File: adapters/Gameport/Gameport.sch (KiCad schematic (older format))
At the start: 20 parts, among them J1 Port 1, J2 Port 2, J3 Gameport, M1 Mounting, M2 Mounting, M3 Mounting, M4 Mounting, Q1 BC557, Q2 BC557

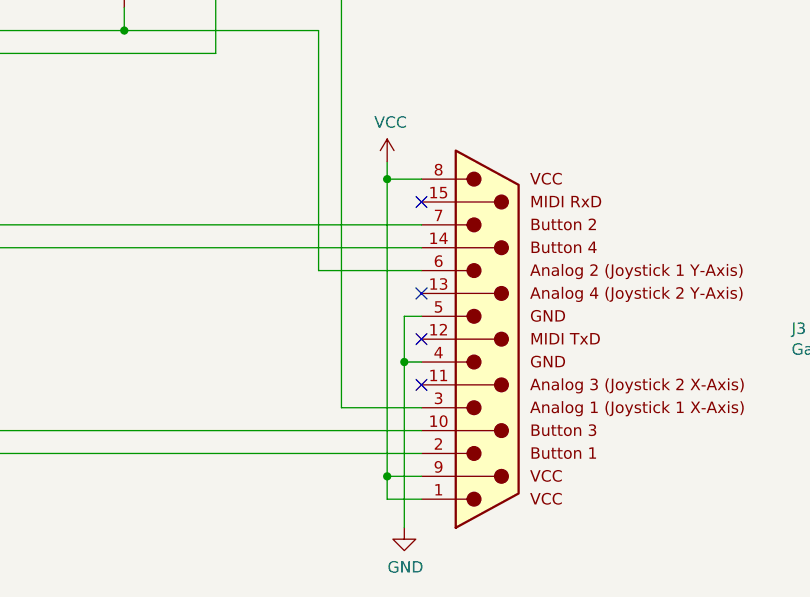
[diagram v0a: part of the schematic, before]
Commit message: Fixed pin linked to VCC
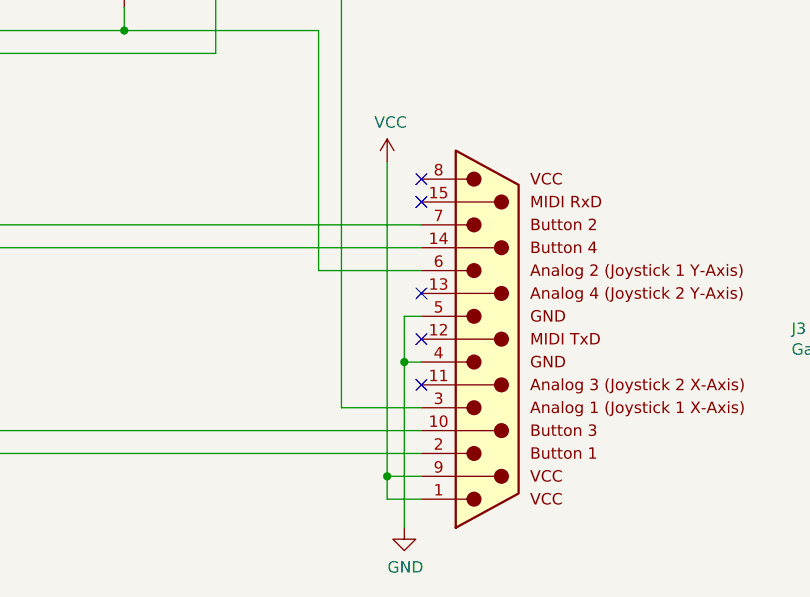
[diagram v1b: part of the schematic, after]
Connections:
- net VCC: no longer J3.8 (VCC)
- no-connect marks 13 -> 14
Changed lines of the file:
@@
 Rev "A"
 Comp ""
-Comment1 "Adapter is untested!"
+Comment1 ""
 Comment2 "Gravis gamepad makes this a viable option for many games."
 Comment3 "gameport. While originally an analog controller, the adoption of gamepads such as the"
@@
 	1    0    0    -1
 $EndComp
-Wire Wire Line
-	8450 4450 8450 4375
 $Comp
 L pc_gameport:Gameport_DB15 J3
@@
 $EndComp
 Wire Wire Line
-	8450 4450 8450 5750
-Connection ~ 8450 4450
-Wire Wire Line
 	8450 5750 8450 5850
 Connection ~ 8450 5750
-Wire Wire Line
-	8450 4450 8600 4450
 Wire Wire Line
 	8450 5750 8600 5750
@@
 Wire Wire Line
 	3025 1550 3025 1950
+Wire Wire Line
+	8450 4375 8450 5750
+NoConn ~ 8600 4450
 $EndSCHEMATC

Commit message: Trying out different circuit
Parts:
- removed Q1, Q2: BC557, Package_TO_SOT_THT:TO-92_Inline_Wide, symbol Transistor_BJT:BC557
- removed RV1, RV2: 100k, RM-065:RM-065, symbol Device:R_POT
- added Q1, Q2: 2N3906, Package_TO_SOT_THT:TO-92_Inline_Wide, symbol Transistor_BJT:2N3906
- added R7, R8: 100k, resistor:R_Axial_DIN0207_L6.3mm_D2.5mm_P7.62mm_Horizontal, symbol Device:R
- R1, R2: value 2k2 -> 100k
- R5, R6: value 2k2 -> 47k
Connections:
- net JK_DOWN: now also R2.2; no longer R6.2
- net JK_LEFT: now also R5.1; no longer R1.2, R3.2
- net JK_RIGHT: now also R1.2; no longer R5.2
- net JK_UP: now also R6.2; no longer R2.2, R4.2
- net VCC: now also R3.1, R4.1, Q1.1 (E), Q2.1 (E), R7.1, R8.1; no longer J3.9 (VCC), R5.1, R6.1
- net at J3.3 (A1): now also D1.1 (K), R3.2, Q1.3 (C)
- net at J3.6 (A2): now also D2.1 (K), R4.2, Q2.3 (C)
- new net: Q1.2 (B), R5.2, R7.2
- new net: Q2.2 (B), R6.1, R8.2
- no-connect marks 14 -> 15

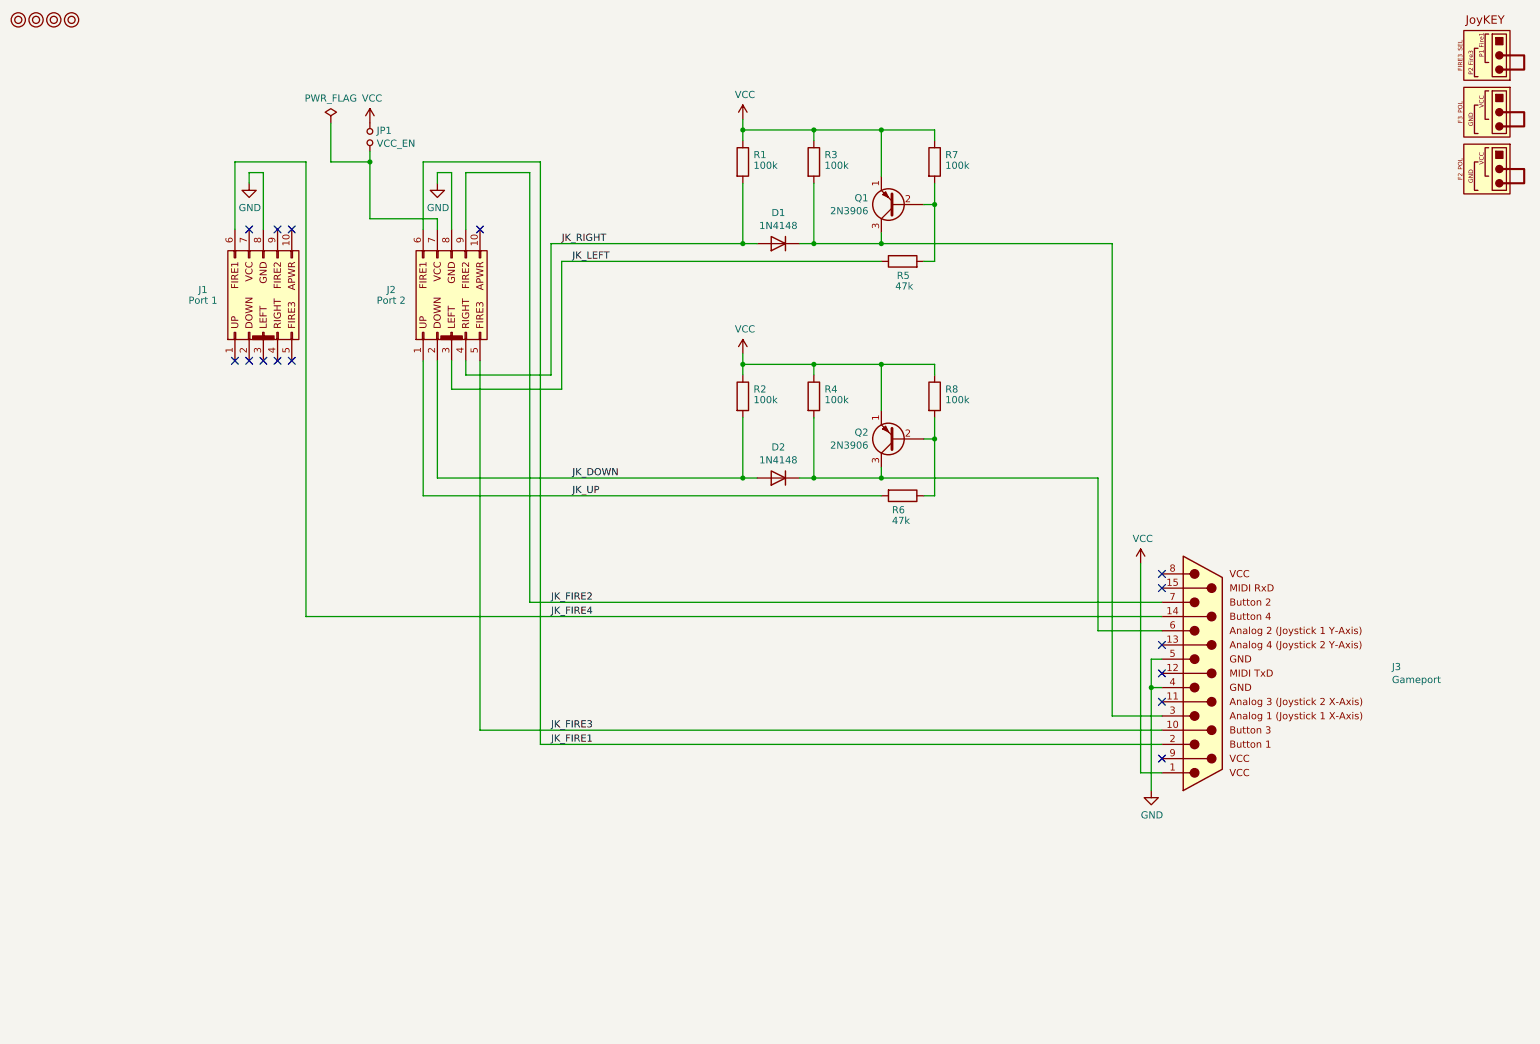
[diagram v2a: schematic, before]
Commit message: Different gameport circuit
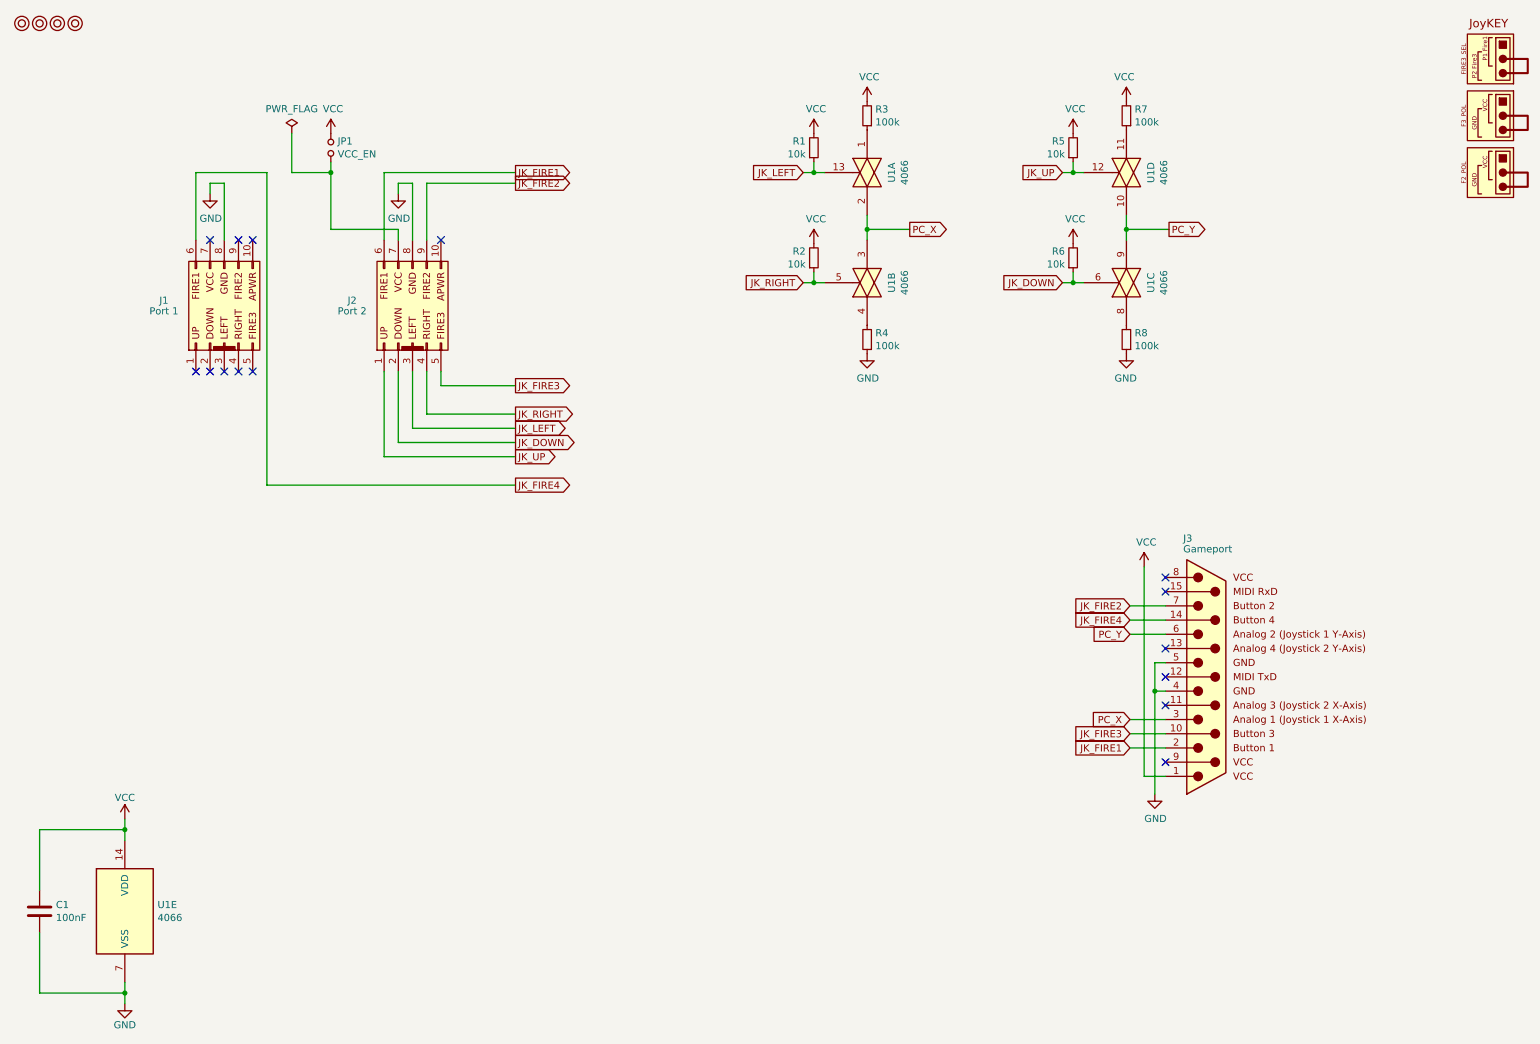
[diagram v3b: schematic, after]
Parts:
- removed D1, D2: 1N4148, Diode_THT:D_DO-35_SOD27_P7.62mm_Horizontal, symbol Diode:1N4148
- removed Q1, Q2: 2N3906, Package_TO_SOT_THT:TO-92_Inline_Wide, symbol Transistor_BJT:2N3906
- removed R1, R2, R3, R4, R7, R8: 100k, resistor:R_Axial_DIN0207_L6.3mm_D2.5mm_P7.62mm_Horizontal, symbol Device:R
- removed R5, R6: 47k, resistor:R_Axial_DIN0207_L6.3mm_D2.5mm_P7.62mm_Horizontal, symbol Device:R
- added C1: 100nF, Capacitor_THT:C_Disc_D4.7mm_W2.5mm_P5.00mm, symbol Device:C
- added R1, R2, R5, R6: 10k, Resistor_THT:R_Axial_DIN0207_L6.3mm_D2.5mm_P10.16mm_Horizontal, symbol Device:R_Small
- added R3, R4, R7, R8: 100k, Resistor_THT:R_Axial_DIN0207_L6.3mm_D2.5mm_P10.16mm_Horizontal, symbol Device:R_Small
- added U1: 4066, Package_DIP:DIP-14_W7.62mm_Socket_LongPads, symbol 4xxx:4066
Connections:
- net GND: now also C1.2, R4.1, R8.1, U1.7 (VSS)
- net JK_DOWN: now also R6.1, U1.6
- net JK_LEFT: now also R1.1, U1.13
- net JK_RIGHT: now also R2.1, U1.5
- net JK_UP: now also R5.1, U1.12
- net VCC: now also C1.1, R1.2, R2.2, R3.2, R5.2, R6.2, R7.2, U1.14 (VDD)
- net PC_X: now reaches J3.3 (A1)
- net PC_X: now also U1.2, U1.3
- net PC_Y: now reaches J3.6 (A2)
- net PC_Y: now also U1.10, U1.9
- new net: R3.1, U1.1
- new net: R4.2, U1.4
- new net: R8.2, U1.8
- new net: R7.1, U1.11
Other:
- moved on the sheet: J1, J2, J3, JP1

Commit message: Gameport adapter that doesn't work
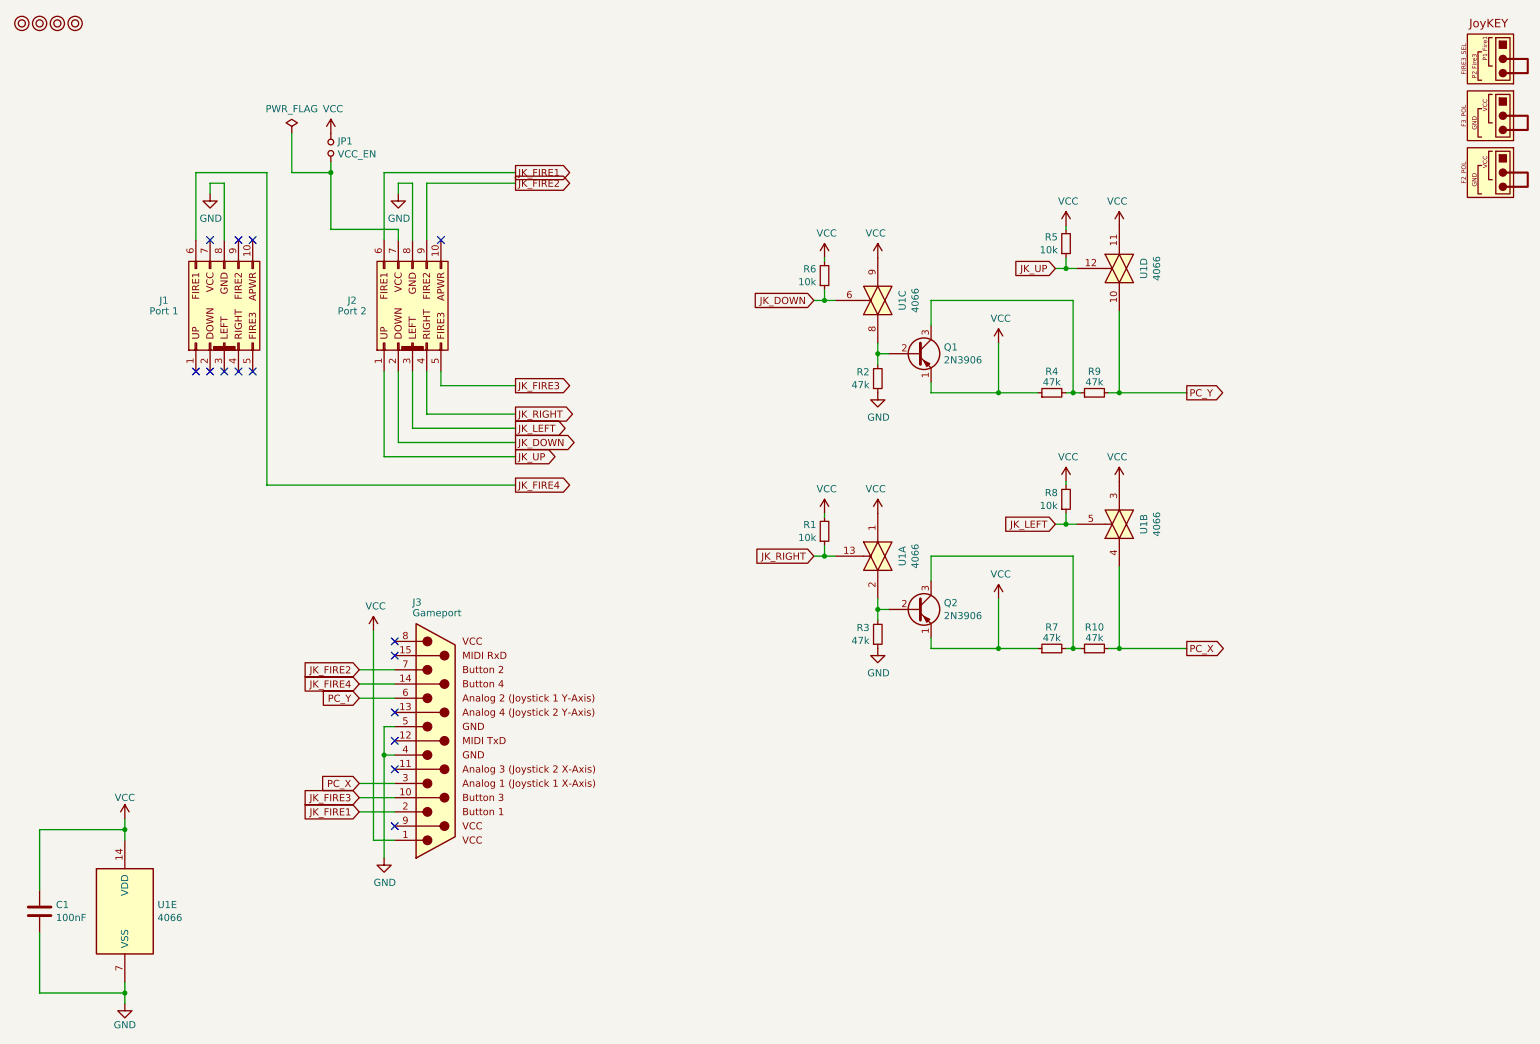
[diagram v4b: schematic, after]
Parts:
- added Q1, Q2: 2N3906, Package_TO_SOT_THT:TO-92_Inline_Wide, symbol Transistor_BJT:2N3906
- added R10, R9: 47k, Resistor_THT:R_Axial_DIN0207_L6.3mm_D2.5mm_P10.16mm_Horizontal, symbol Device:R_Small
- R2: value 10k -> 47k
- R3, R4, R7: value 100k -> 47k
- R8: value 100k -> 10k
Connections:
- net GND: now also R2.1, R3.1; no longer R4.1, R8.1
- net JK_LEFT: now also R8.1, U1.5; no longer R1.1, U1.13
- net JK_RIGHT: now also R1.1, U1.13; no longer R2.1, U1.5
- net PC_X: now also U1.4, R10.2; no longer U1.2, U1.3
- net PC_Y: now also R9.2; no longer U1.9
- net VCC: now also R4.1, R7.1, R8.2, U1.1, U1.11, U1.3, U1.9, Q1.1 (E), Q2.1 (E); no longer R2.2, R3.2, R7.2
- net at R4.2: now also Q1.3 (C), R9.1; no longer U1.4
- net at U1.8: now also R2.2, Q1.2 (B); no longer R8.2
- new net: Q2.2 (B), R3.2, U1.2
- new net: Q2.3 (C), R10.1, R7.2
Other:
- moved on the sheet: J3, R5, R6, U1A, U1B, U1C, U1D
